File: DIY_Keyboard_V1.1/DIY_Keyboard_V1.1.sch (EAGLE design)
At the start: 176 parts, among them Y1 16MHz

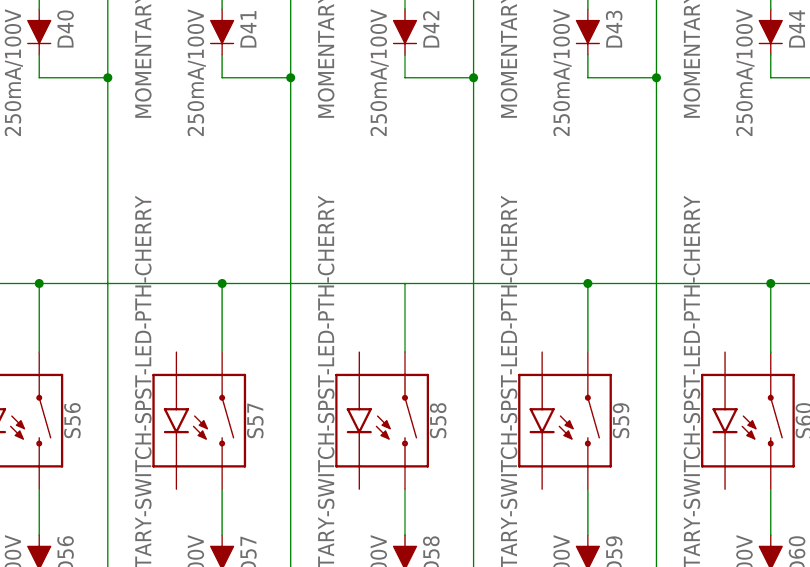
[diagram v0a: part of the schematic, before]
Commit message: Updated connections
Cleared all airwire and clearance errors
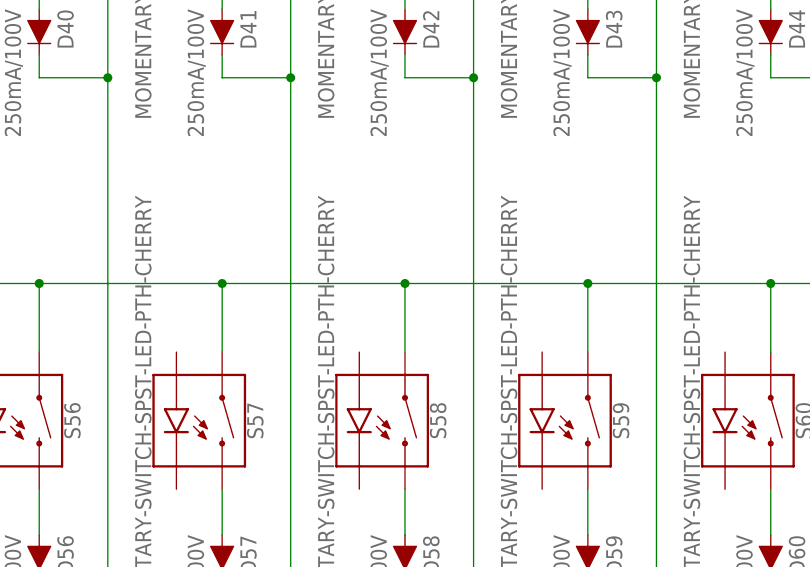
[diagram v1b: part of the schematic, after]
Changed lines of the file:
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@@
 <junction x="320.04" y="-83.82"/>
 <label x="20.32" y="-83.82" size="1.778" layer="95" rot="R180" xref="yes"/>
+<junction x="177.8" y="-83.82"/>
 </segment>
 <segment>

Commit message: Version 1.1 done!!
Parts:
- R3, R4: value 56k -> 5.1k
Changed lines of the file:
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@@
 <part name="ISP" library="SparkFun-Connectors" deviceset="CONN_03X2" device="FEMALE"/>
 <part name="U$1" library="USB-TYPE-C-V2" deviceset="USB_TYPE_C" device=""/>
-<part name="R3" library="SparkFun-Resistors" deviceset="56KOHM" device="" value="56k"/>
-<part name="R4" library="SparkFun-Resistors" deviceset="56KOHM" device="" value="56k"/>
+<part name="R3" library="SparkFun-Resistors" deviceset="56KOHM" device="" value="5.1k"/>
+<part name="R4" library="SparkFun-Resistors" deviceset="56KOHM" device="" value="5.1k"/>
 <part name="D80" library="SparkFun-LED" deviceset="LED-WHITE" device="0603" value="WHITE"/>
 <part name="R5" library="SparkFun-Resistors" deviceset="22OHM" device="-0603-1/10W-1%" value="22"/>
